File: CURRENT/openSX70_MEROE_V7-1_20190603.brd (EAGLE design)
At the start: 95.9 x 27.9 mm, 43 parts, among them J1 687106183722, Q1 5.8A/30V/35mΩ, Q2 5.8A/30V/35mΩ, U1 ATMEGA328P_TQFP, U2 TPS79501DCQ, Y1 CSTCE8M00G52Z-R0

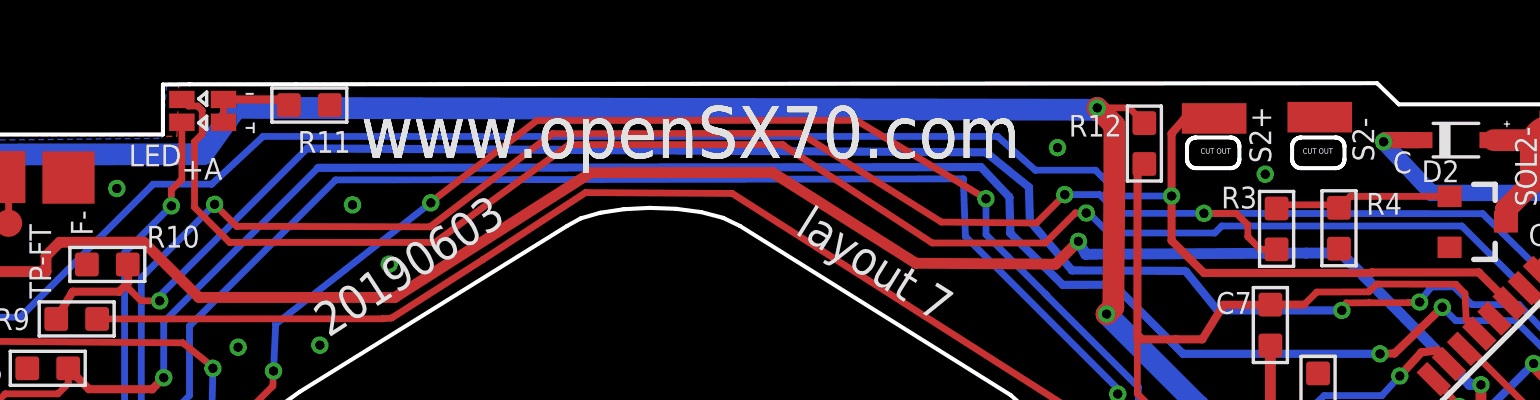
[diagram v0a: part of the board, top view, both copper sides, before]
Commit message: NEW RAISED LEDs
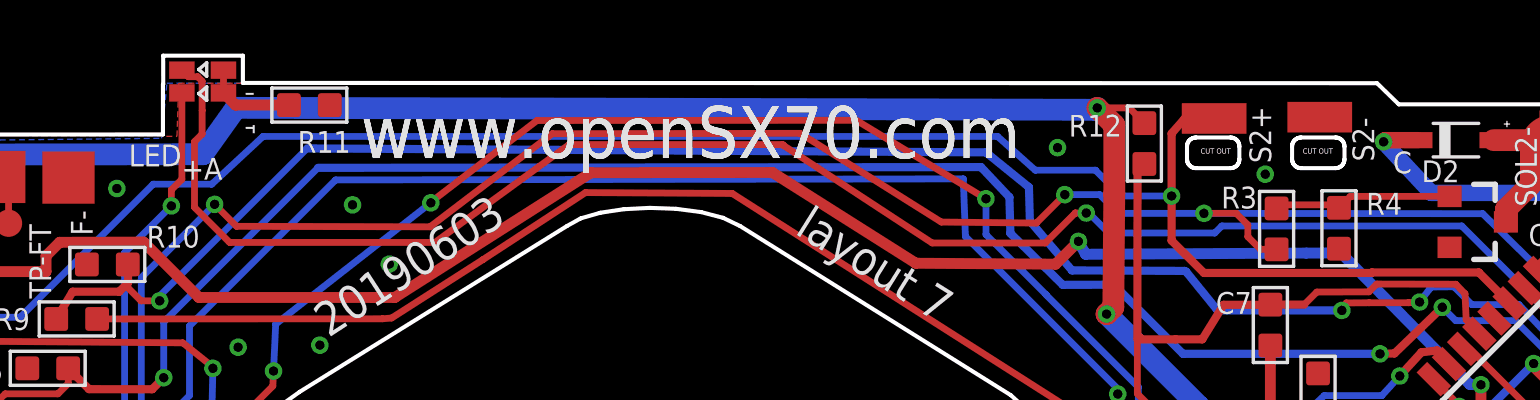
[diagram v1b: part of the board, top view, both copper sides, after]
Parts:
- moved U$4 1.09 mm to (30.0, 28.7)
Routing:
- net LED2: track 62.4 -> 63.5 mm
- net LED1: track 100.4 -> 101.5 mm
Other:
- board size 95.9 x 27.9 mm -> 95.9 x 28.9 mm
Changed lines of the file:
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@@
 <wire x1="17.1616" y1="26.7473" x2="28.4899" y2="26.7557" width="0.1524" layer="20"/>
 <wire x1="28.4899" y1="26.7557" x2="28.4899" y2="28.6155" width="0.1524" layer="20"/>
-<wire x1="28.4899" y1="28.6155" x2="29.4908" y2="28.6258" width="0.1524" layer="20"/>
-<wire x1="29.4908" y1="28.6258" x2="33.4518" y2="28.6258" width="0.1524" layer="20"/>
-<wire x1="33.4518" y1="28.6258" x2="73.7652" y2="28.6663" width="0.1524" layer="20"/>
+<wire x1="28.4899" y1="28.6155" x2="28.5002" y2="28.6258" width="0.1524" layer="20"/>
+<wire x1="28.5002" y1="28.6258" x2="28.4988" y2="29.6926" width="0.1524" layer="20"/>
+<wire x1="28.4988" y1="29.6926" x2="31.4706" y2="29.6926" width="0.1524" layer="20"/>
+<wire x1="31.4706" y1="29.6926" x2="31.4706" y2="28.6766" width="0.1524" layer="20"/>
+<wire x1="31.4706" y1="28.6766" x2="73.7652" y2="28.6663" width="0.1524" layer="20"/>
 <wire x1="73.7652" y1="28.6663" x2="74.576" y2="27.8772" width="0.1524" layer="20"/>
 <wire x1="74.576" y1="27.8772" x2="91.6056" y2="27.8772" width="0.1524" layer="20"/>
@@
 <text x="14.3002" y="7.1374" size="0.8128" layer="21" font="vector" ratio="20">6V</text>
 <text x="16.6116" y="10.541" size="0.8128" layer="21" font="vector" ratio="20" rot="R180">3.3V</text>
-<wire x1="31.8754" y1="26.9988" x2="31.8754" y2="27.202" width="0.0762" layer="21" style="shortdash"/>
+<wire x1="31.8754" y1="26.8004" x2="31.8754" y2="27.202" width="0.0762" layer="21" style="shortdash"/>
 <wire x1="31.8736" y1="26.9986" x2="31.5736" y2="26.9986" width="0.0762" layer="21" style="shortdash"/>
-<wire x1="31.8754" y1="26.8004" x2="31.8754" y2="26.9988" width="0.0762" layer="21" style="shortdash"/>
 <wire x1="31.8736" y1="28.2686" x2="31.5736" y2="28.2686" width="0.0762" layer="21" style="shortdash"/>
 </plain>
@@
 </element>
 <element name="U$1" library="_openSX70" library_urn="urn:adsk.eagle:library:7902803" package="SX70-7-PAD-PROPER" package3d_urn="urn:adsk.eagle:package:7902942/1" value="SX70-7-PAD" x="89.154" y="17.3228" smashed="yes" rot="R296"/>
-<element name="U$4" library="LTST-C195KGJRKT" package="LTST-BILED-15X16" value="LTST-C195KGJRKT" x="29.972" y="27.6352" smashed="yes" rot="R270">
-<attribute name="AVAILABILITY" value="Unavailable" x="29.972" y="27.6352" size="1.778" layer="27" rot="R270" display="off"/>
-<attribute name="DESCRIPTION" value=" Green/Red 130° Water Clear 35/25 mcd 2 V 0605 Surface Mount Bi-Color LED " x="29.972" y="27.6352" size="1.778" layer="27" rot="R270" display="off"/>
-<attribute name="MF" value="Lite-On Inc." x="29.972" y="27.6352" size="1.778" layer="27" rot="R270" display="off"/>
-<attribute name="MP" value="LTST-C195KGJRKT" x="29.972" y="27.6352" size="1.778" layer="27" rot="R270" display="off"/>
-<attribute name="PACKAGE" value="0606 Lite-On" x="29.972" y="27.6352" size="1.778" layer="27" rot="R270" display="off"/>
-<attribute name="PRICE" value="None" x="29.972" y="27.6352" size="1.778" layer="27" rot="R270" display="off"/>
+<element name="U$4" library="LTST-C195KGJRKT" package="LTST-BILED-15X16" value="LTST-C195KGJRKT" x="29.972" y="28.7274" smashed="yes" rot="R270">
+<attribute name="AVAILABILITY" value="Unavailable" x="29.972" y="28.7274" size="1.778" layer="27" rot="R270" display="off"/>
+<attribute name="DESCRIPTION" value=" Green/Red 130° Water Clear 35/25 mcd 2 V 0605 Surface Mount Bi-Color LED " x="29.972" y="28.7274" size="1.778" layer="27" rot="R270" display="off"/>
+<attribute name="MF" value="Lite-On Inc." x="29.972" y="28.7274" size="1.778" layer="27" rot="R270" display="off"/>
+<attribute name="MP" value="LTST-C195KGJRKT" x="29.972" y="28.7274" size="1.778" layer="27" rot="R270" display="off"/>
+<attribute name="PACKAGE" value="0606 Lite-On" x="29.972" y="28.7274" size="1.778" layer="27" rot="R270" display="off"/>
+<attribute name="PRICE" value="None" x="29.972" y="28.7274" size="1.778" layer="27" rot="R270" display="off"/>
 </element>
 <element name="TP1" library="SparkFun-Connectors" package="PAD.03X.04" value="TEST-POINT3X4" x="22.733" y="23.4442" smashed="yes"/>
@@
 <element name="C4" library="Seeed-Capacitor" package="C0603" value="1uf" x="17.8308" y="10.8712" smashed="yes">
 <attribute name="MPN" value="CC0603KRX5R6BB106" x="17.8308" y="10.8712" size="1.778" layer="27" display="off"/>
+<attribute name="NAME" x="17.5768" y="12.1412" size="0.635" layer="33" ratio="10" rot="R270"/>
 <attribute name="NAME" x="18.9484" y="11.5062" size="0.8128" layer="25" font="vector" ratio="20"/>
-<attribute name="NAME" x="17.5768" y="12.1412" size="0.635" layer="33" ratio="10" rot="R270"/>
 <attribute name="VALUE" x="16.2433" y="12.1412" size="0.635" layer="27" ratio="10" rot="R270"/>
 </element>
@@
 <element name="C3" library="Seeed-Capacitor" package="C0603" value="100nf" x="13.843" y="20.5994" smashed="yes" rot="MR90">
 <attribute name="MPN" value="CC0603KRX7R9BB104" x="13.843" y="20.5994" size="1.778" layer="28" rot="MR90" display="off"/>
+<attribute name="NAME" x="15.113" y="20.3454" size="0.635" layer="34" ratio="10" rot="MR0"/>
 <attribute name="NAME" x="12.1666" y="20.4216" size="0.6096" layer="26" font="vector" ratio="11" rot="MR0"/>
-<attribute name="NAME" x="15.113" y="20.3454" size="0.635" layer="34" ratio="10" rot="MR0"/>
 <attribute name="VALUE" x="15.113" y="19.0119" size="0.635" layer="28" ratio="10" rot="MR0"/>
 </element>
@@
 <wire x1="70.647225" y1="4.4072" x2="67.636821875" y2="1.524" width="0.254" layer="1"/>
 <contactref element="U$4" pad="P$3"/>
-<wire x1="29.1962" y1="27.2102" x2="29.1962" y2="25.0812" width="0.254" layer="1"/>
+<wire x1="29.1962" y1="28.3024" x2="29.1962" y2="25.0812" width="0.254" layer="1"/>
 <wire x1="29.1962" y1="25.0812" x2="28.805" y2="24.69" width="0.254" layer="1"/>
 </signal>
@@
 <contactref element="U$4" pad="P$2"/>
 <contactref element="R11" pad="2"/>
-<wire x1="30.7478" y1="28.0602" x2="30.7478" y2="27.2102" width="0.254" layer="1"/>
-<wire x1="30.7478" y1="28.0602" x2="32.9772" y2="28.0602" width="0.3048" layer="1"/>
-<wire x1="32.9772" y1="28.0602" x2="33.1872" y2="27.8502" width="0.3048" layer="1"/>
+<wire x1="30.7478" y1="29.1524" x2="30.7478" y2="28.3024" width="0.254" layer="1"/>
+<wire x1="30.7478" y1="28.3024" x2="31.2" y2="27.8502" width="0.4064" layer="1"/>
+<wire x1="31.2" y1="27.8502" x2="33.1872" y2="27.8502" width="0.4064" layer="1"/>
 </signal>
 <signal name="LED2">
@@
 <wire x1="38.633934375" y1="22.7284" x2="43.63725625" y2="26.3775375" width="0.254" layer="1"/>
 <wire x1="76.925290625" y1="23.3426" x2="67.97765" y2="23.3426" width="0.254" layer="16"/>
-<wire x1="29.78773125" y1="27.8146" x2="29.9514" y2="27.65093125" width="0.254" layer="1"/>
 <wire x1="29.9514" y1="27.65093125" x2="29.9514" y2="26.76946875" width="0.254" layer="1"/>
-<wire x1="29.1962" y1="28.0602" x2="29.4418" y2="27.8146" width="0.254" layer="1"/>
-<wire x1="29.4418" y1="27.8146" x2="29.78773125" y2="27.8146" width="0.254" layer="1"/>
 <wire x1="29.9514" y1="26.76946875" x2="29.6672" y2="26.48526875" width="0.254" layer="1"/>
 <wire x1="30.97745" y1="22.7284" x2="38.633934375" y2="22.7284" width="0.254" layer="1"/>
 <wire x1="29.6672" y1="24.03865" x2="30.97745" y2="22.7284" width="0.254" layer="1"/>
 <wire x1="29.6672" y1="26.48526875" x2="29.6672" y2="24.03865" width="0.254" layer="1"/>
+<wire x1="29.1962" y1="29.1524" x2="29.4418" y2="28.9068" width="0.254" layer="1"/>
+<wire x1="29.4418" y1="28.9068" x2="29.78773125" y2="28.9068" width="0.254" layer="1"/>
+<wire x1="29.78773125" y1="28.9068" x2="29.9514" y2="28.74313125" width="0.254" layer="1"/>
+<wire x1="29.9514" y1="28.74313125" x2="29.9514" y2="27.65093125" width="0.254" layer="1"/>
 </signal>
 <signal name="N$10">
